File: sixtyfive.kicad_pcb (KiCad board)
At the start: 2 copper layers, 305 x 100.3 mm, 170 parts, among them J1 Conn_01x12, J2 Conn_ARM_JTAG_SWD_10, Q1 BSS138, SW1 SW_Push, U1 USBLC6-2SC6, U2 STM32F072C8Tx, U3 MCP1700-3302E_SOT23

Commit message: More routing changes, pulled things away from the edge and added more ground plane vias
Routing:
- net BOOT0: track 223.2 -> 210.7 mm
- net NRST: track 215.8 -> 208.2 mm
- net SWCLK: track 159.3 -> 152.2 mm
- net SWDIO: track 156.4 -> 150.0 mm
- net 3.3V: track 232.9 -> 236.1 mm
- net GND: vias 4 -> 25

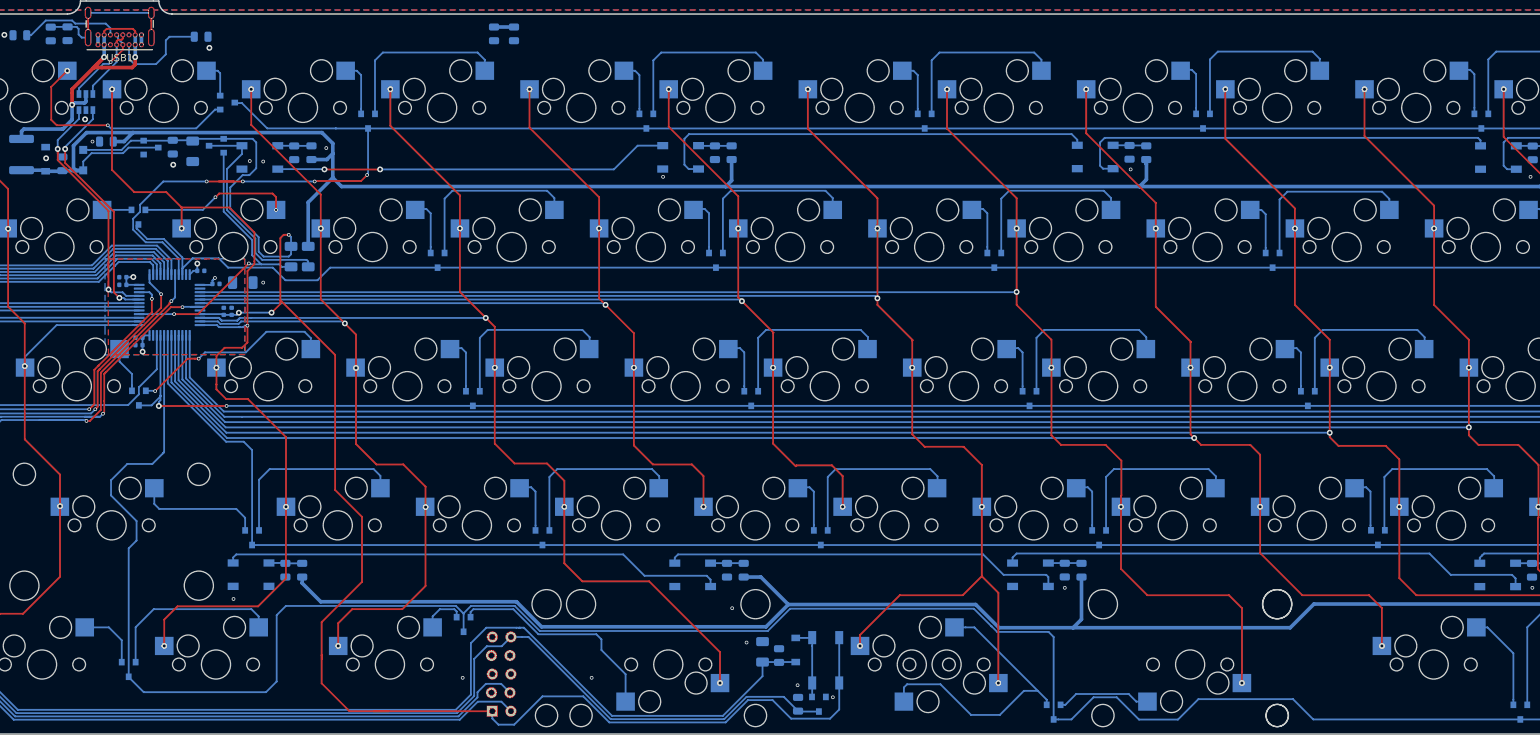
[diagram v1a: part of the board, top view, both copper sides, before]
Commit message: swapped a couple components for basic parts, rerouted
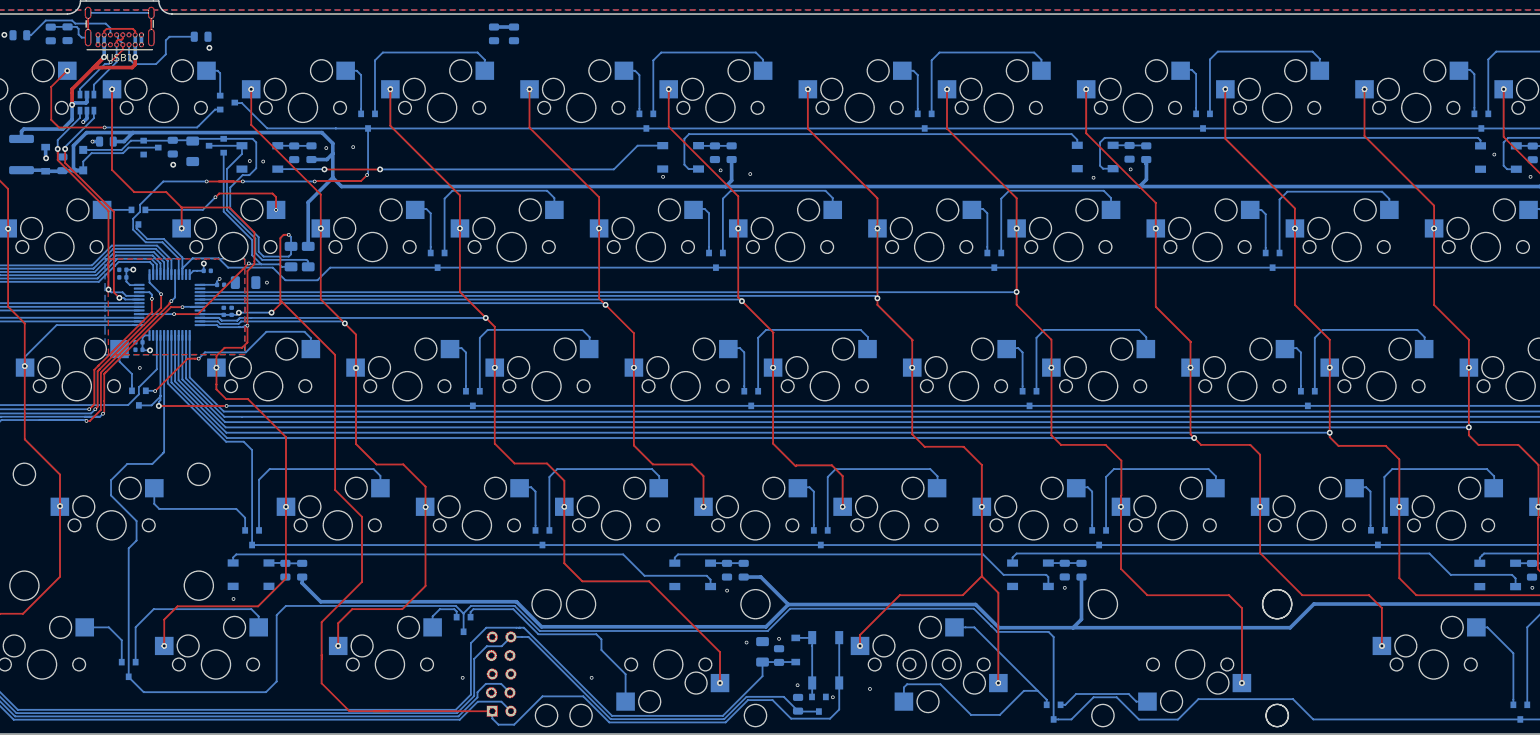
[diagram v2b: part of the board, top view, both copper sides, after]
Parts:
- U1: value USBLC6-2SC6 -> SRV05-4
- moved CB4 1.02 mm to (290.0, 273.1)
- moved CB8 1.02 mm to (290.0, 274.1)
- moved CB5 0.89 mm to (301.6, 273.2)
- moved CB1 0.65 mm to (303.4, 275.1)
- moved CB6 0.63 mm to (292.2, 283.0)
- moved CB7 0.63 mm to (292.2, 284.0)
- moved RGND1 0.38 mm to (306.8, 274.8)
- moved U1 0.16 mm to (285.1, 250.2)
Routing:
- net GND: track 2.70 -> 6.99 mm, vias 25 -> 33
- net 3.3V: track 236.1 -> 239.1 mm

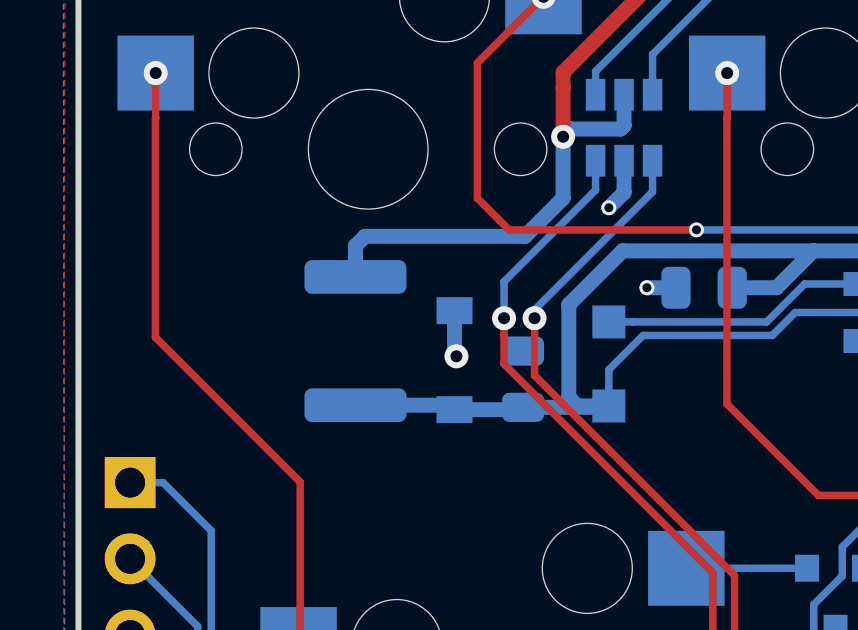
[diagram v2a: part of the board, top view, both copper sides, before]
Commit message: Didn't quite save everything that last time.
Just following the last bit of advice from the discord, swapping a couple components and rerouting some things
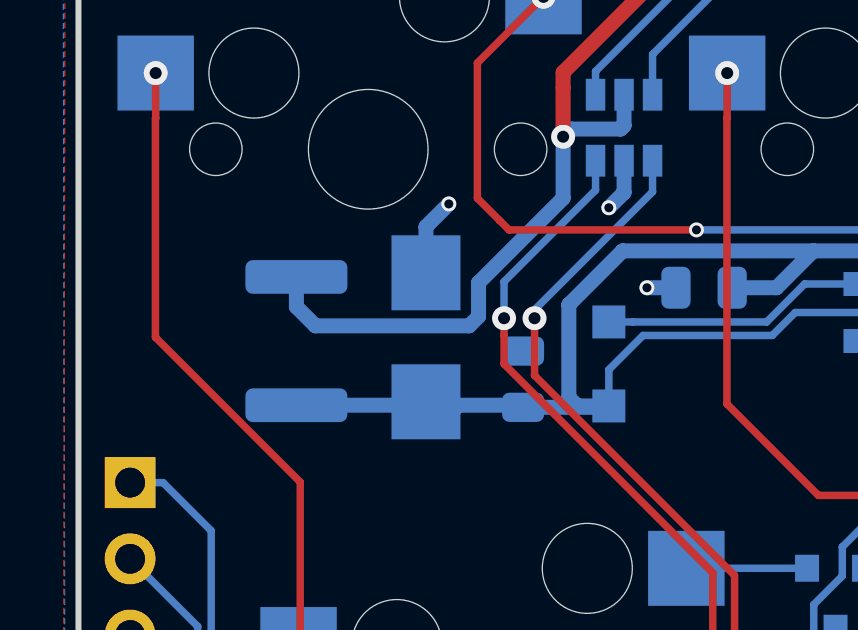
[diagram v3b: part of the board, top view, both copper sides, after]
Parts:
- DF1: value SMF9.0CA -> P6SMB6.8CA; footprint Diode_SMD:D_SOD-123 -> Diode_SMD:D_SMB
- moved F1 1.97 mm to (274.2, 257.3)
- moved DF1 1.22 mm to (278.5, 257.2)
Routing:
- net VBUS: track 42.8 -> 46.8 mm
- net 5V: track 662.6 -> 664.8 mm
- net GND: track 6.99 -> 8.06 mm

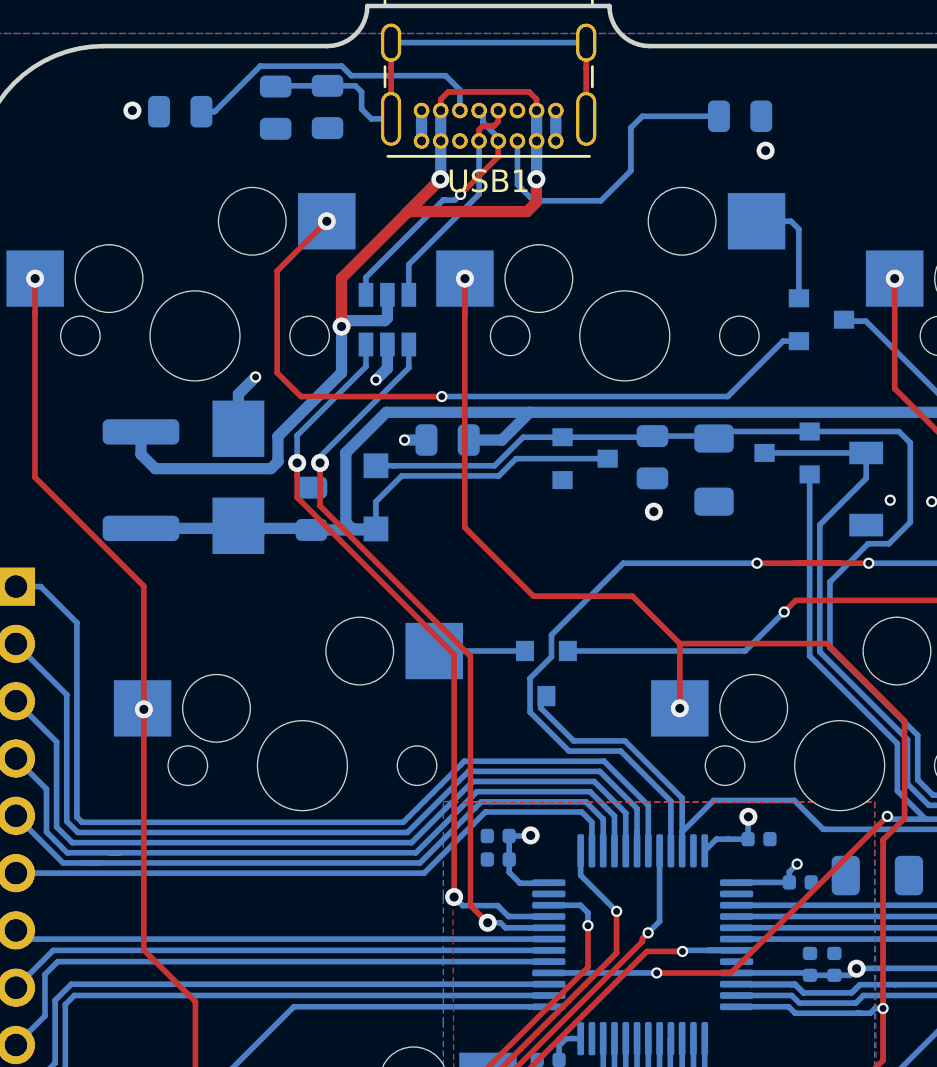
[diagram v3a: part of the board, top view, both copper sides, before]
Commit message: Further discord feedback, using the srv05 properly now
using the component right this time
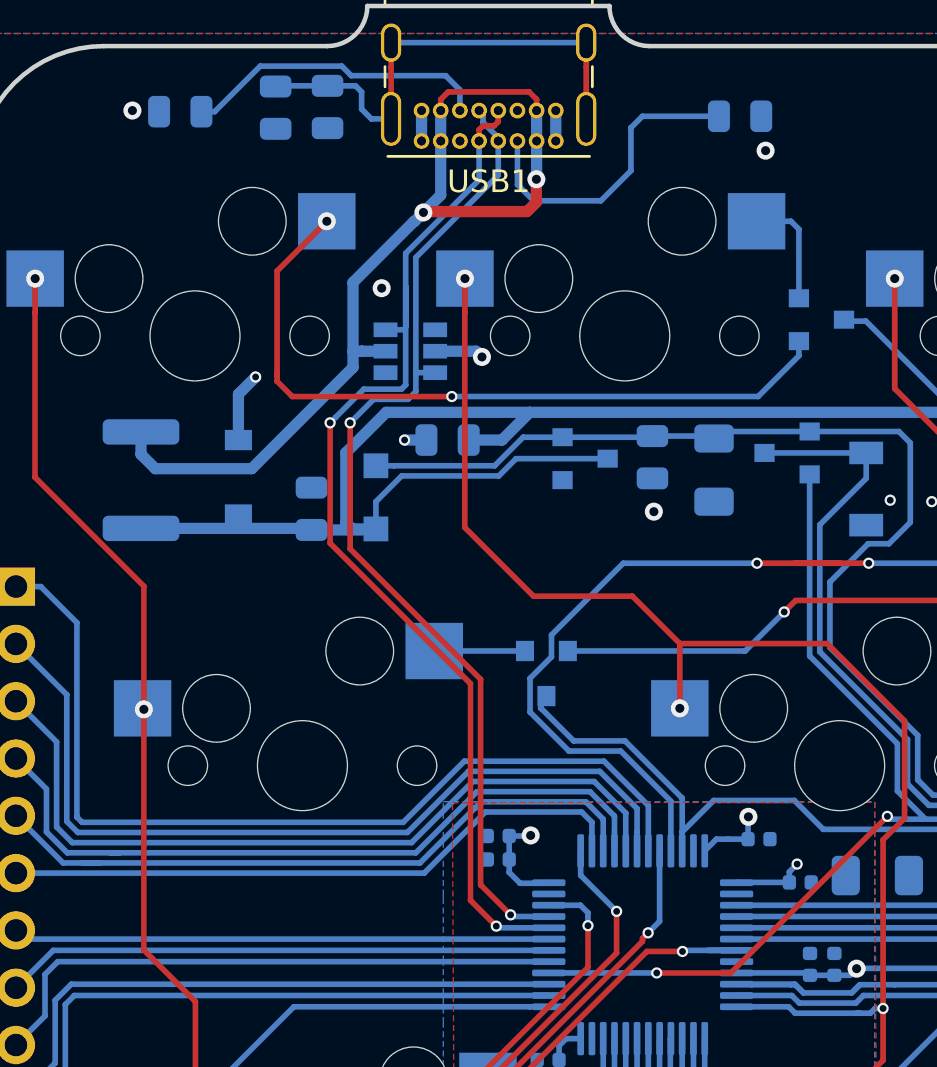
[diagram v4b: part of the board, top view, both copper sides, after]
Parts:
- DF1: footprint Diode_SMD:D_SMB -> Diode_SMD:D_SOD-123
- moved U1 1.73 mm to (286.1, 251.6), turned to 180 degrees
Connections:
- U1 pad 1: D- -> Net-(U1-Pad1)
- U1 pad 4: DBus+ -> Net-(U1-Pad4)
- U1 pad 6: DBus- -> D-
- USB1 pad A6: DBus+ -> D+
- USB1 pad A7: DBus- -> D-
- USB1 pad B6: DBus+ -> D+
- USB1 pad B7: DBus- -> D-
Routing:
- net D-: track 33.1 -> 48.4 mm
- net D+: track 33.4 -> 45.2 mm
- net DBus+: track 11.3 -> 0.00 mm, vias 1 -> 0
- net DBus-: track 10.1 -> 0.00 mm
- net VBUS: track 46.8 -> 41.8 mm, vias 3 -> 2
- net Net-(D1-Pad1): track 32.2 -> 32.8 mm
- net GND: track 8.06 -> 8.46 mm, vias 33 -> 34

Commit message: Added some decoration, changed the connector and rerouted a tiny bit
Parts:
- removed RSO1: 100k, Resistor_SMD:R_1206_3216Metric
- added ?: , , F.Cu at (104.0, 292.6)
- added G***: LOGO, sixtyfive:nicole_x, F.Cu at (559.9, 250.4)
- added G***: LOGO, sixtyfive:nicole_x, B.Cu at (559.9, 250.6)
- added M2: MountingHole_2.2mm_M2, MountingHole:MountingHole_2.2mm_M2, B.Cu at (290.6, 295.5)
- added M2: MountingHole_2.2mm_M2, MountingHole:MountingHole_2.2mm_M2, B.Cu at (557.5, 314.9)
- added M2: MountingHole_2.2mm_M2, MountingHole:MountingHole_2.2mm_M2, B.Cu at (314.4, 326.7)
- added M2: MountingHole_2.2mm_M2, MountingHole:MountingHole_2.2mm_M2, B.Cu at (457.6, 326.7)
- added M2: MountingHole_2.2mm_M2, MountingHole:MountingHole_2.2mm_M2, B.Cu at (548.4, 279.5)
- added M2: MountingHole_2.2mm_M2, MountingHole:MountingHole_2.2mm_M2, B.Cu at (516.6, 241.4)
- added M2: MountingHole_2.2mm_M2, MountingHole:MountingHole_2.2mm_M2, B.Cu at (306.4, 241.4)
- DF1: footprint Diode_SMD:D_SOD-123 -> Diode_SMD:D_SMB
- J2: value Conn_ARM_JTAG_SWD_10 -> STLINK_6_Pin; footprint sixtyfive:Conn_ARM_JTAG_SWD_10 -> Connectors:2X3_LOCK
- moved CSO1 2.98 mm to (299.8, 256.3)
- moved J2 2.27 mm to (343.6, 329.8), turned to 180 degrees
- moved D29 0.38 mm to (291.2, 327.8)
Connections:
- J2 pad 2: SWDIO -> NRST
- J2 pad 6: Net-(J2-Pad6) -> SWDIO
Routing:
- net BOOT0: track 210.7 -> 207.2 mm
- net Col1: track 105.9 -> 109.1 mm
- net Net-(D30-Pad2): track 30.4 -> 27.8 mm
- net SWCLK: track 152.2 -> 154.6 mm
- net D-: track 48.4 -> 46.7 mm
- net 3.3V: track 239.1 -> 240.7 mm, vias 7 -> 8
- net Row4: track 279.7 -> 280.3 mm
- net SWDIO: track 150.0 -> 149.3 mm
- net Col9: track 251.9 -> 251.3 mm
- net Row2: track 239.1 -> 238.5 mm
- net GND: vias 34 -> 35
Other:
- board text added: "3.3V"
- board text added: "GND"
- board text added: "NRST"
- board text added: "SWCLK"
- board text added: "SWDIO"
- board text added: "nicole aptekar"
- board text added: "sixtyfive"

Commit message: Moved one diode
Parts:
- moved D34 2.67 mm to (566.8, 331.0)
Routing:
- net Net-(D34-Pad1): track 11.8 -> 8.90 mm
- net Net-(D34-Pad2): track 50.9 -> 48.5 mm
- net Row5: track 364.9 -> 365.7 mm
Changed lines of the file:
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@@
     (thickness 1.6)
     (drawings 21)
-    (tracks 1554)
+    (tracks 1555)
     (zones 0)
     (modules 179)
@@
   )
   (module Package_TO_SOT_SMD:SOT-23 (layer B.Cu)
-    (at 566.801 333.629 270)
+    (at 566.801 330.962 270)
     (descr "SOT-23, Standard")
     (tags SOT-23)
@@
   (segment (start 534.797 319.786) (end 534.096 320.487) (width 0.25) (layer B.Cu) (net 54))
   (segment (start 549.12895 320.40055) (end 548.5137 319.7853) (width 0.25) (layer B.Cu) (net 54))
-  (segment (start 568.69 332.629) (end 567.751 332.629) (width 0.25) (layer B.Cu) (net 55))
-  (segment (start 569.976 331.343) (end 568.69 332.629) (width 0.25) (layer B.Cu) (net 55))
   (segment (start 568.17895 283.92755) (end 568.17895 285.42755) (width 0.25) (layer B.Cu) (net 55))
   (segment (start 568.17895 285.42755) (end 568.198 285.4466) (width 0.25) (layer B.Cu) (net 55))
   (segment (start 568.198 286.004) (end 569.976 287.782) (width 0.25) (layer B.Cu) (net 55))
   (segment (start 568.198 285.4466) (end 568.198 286.004) (width 0.25) (layer B.Cu) (net 55))
-  (segment (start 569.976 287.782) (end 569.976 331.343) (width 0.25) (layer B.Cu) (net 55))
+  (segment (start 569.071 329.962) (end 569.976 329.057) (width 0.25) (layer B.Cu) (net 55))
+  (segment (start 567.751 329.962) (end 569.071 329.962) (width 0.25) (layer B.Cu) (net 55))
+  (segment (start 569.976 287.782) (end 569.976 329.057) (width 0.25) (layer B.Cu) (net 55))
   (segment (start 347.472 310.753) (end 385.572 310.753) (width 0.25) (layer B.Cu) (net 56))
   (segment (start 385.572 310.753) (end 423.672 310.753) (width 0.25) (layer B.Cu) (net 56))
@@
   (segment (start 307.721 296.61202) (end 306.86199 295.75301) (width 0.25) (layer B.Cu) (net 56))
   (segment (start 307.721 310.753) (end 307.721 296.61202) (width 0.25) (layer B.Cu) (net 56))
-  (segment (start 567.436 334.629) (end 481.33 334.629) (width 0.25) (layer B.Cu) (net 57))
   (segment (start 481.33 334.629) (end 452.993 334.629) (width 0.25) (layer B.Cu) (net 57))
   (segment (start 452.993 334.629) (end 450.215 331.851) (width 0.25) (layer B.Cu) (net 57))
@@
   (segment (start 292.8915 330.8985) (end 293.1795 330.8985) (width 0.25) (layer B.Cu) (net 57))
   (segment (start 293.1795 330.8985) (end 309.626 330.8985) (width 0.25) (layer B.Cu) (net 57))
+  (segment (start 564.834 334.629) (end 550.942 334.629) (width 0.25) (layer B.Cu) (net 57))
+  (segment (start 566.801 332.662) (end 564.834 334.629) (width 0.25) (layer B.Cu) (net 57))
+  (segment (start 566.801 331.962) (end 566.801 332.662) (width 0.25) (layer B.Cu) (net 57))
+  (segment (start 550.942 334.629) (end 481.33 334.629) (width 0.25) (layer B.Cu) (net 57))
   (segment (start 384.3548 323.47) (end 384.3951 323.4297) (width 0.25) (layer B.Cu) (net 58))
   (segment (start 382.143 323.47) (end 384.3548 323.47) (width 0.25) (layer B.Cu) (net 58))
@@
   (segment (start 532.196 331.929) (end 532.196 322.4926) (width 0.25) (layer B.Cu) (net 139))
   (segment (start 532.196 332.629) (end 532.196 331.929) (width 0.25) (layer B.Cu) (net 139))
-  (segment (start 568.17895 324.33895) (end 568.17895 322.02755) (width 0.25) (layer B.Cu) (net 140))
-  (segment (start 567.3979 325.12) (end 568.17895 324.33895) (width 0.25) (layer B.Cu) (net 140))
-  (segment (start 566.928 325.12) (end 567.3979 325.12) (width 0.25) (layer B.Cu) (net 140))
-  (segment (start 565.851 326.197) (end 566.928 325.12) (width 0.25) (layer B.Cu) (net 140))
-  (segment (start 565.851 332.629) (end 565.851 326.197) (width 0.25) (layer B.Cu) (net 140))
+  (segment (start 565.851 326.5399) (end 568.17895 324.21195) (width 0.25) (layer B.Cu) (net 140))
+  (segment (start 565.851 329.962) (end 565.851 326.5399) (width 0.25) (layer B.Cu) (net 140))
+  (segment (start 568.17895 324.21195) (end 568.17895 322.02755) (width 0.25) (layer B.Cu) (net 140))
   (zone (net 2) (net_name 3.3V) (layer F.Cu) (hatch edge 0.508)
     (priority 1)

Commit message: Reorganized Schematic to be easier to read
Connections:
- net 3.3V renamed +3V3
- net Extra13 renamed Net-(U2-Pad2)
